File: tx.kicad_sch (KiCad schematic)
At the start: 52 parts, among them J7 SMA, Q1 PMOS, Q4 2NPN, T2 RF_BALUN, U12 MAX2831, U13 TXIF_BALUN, U16 DPDT

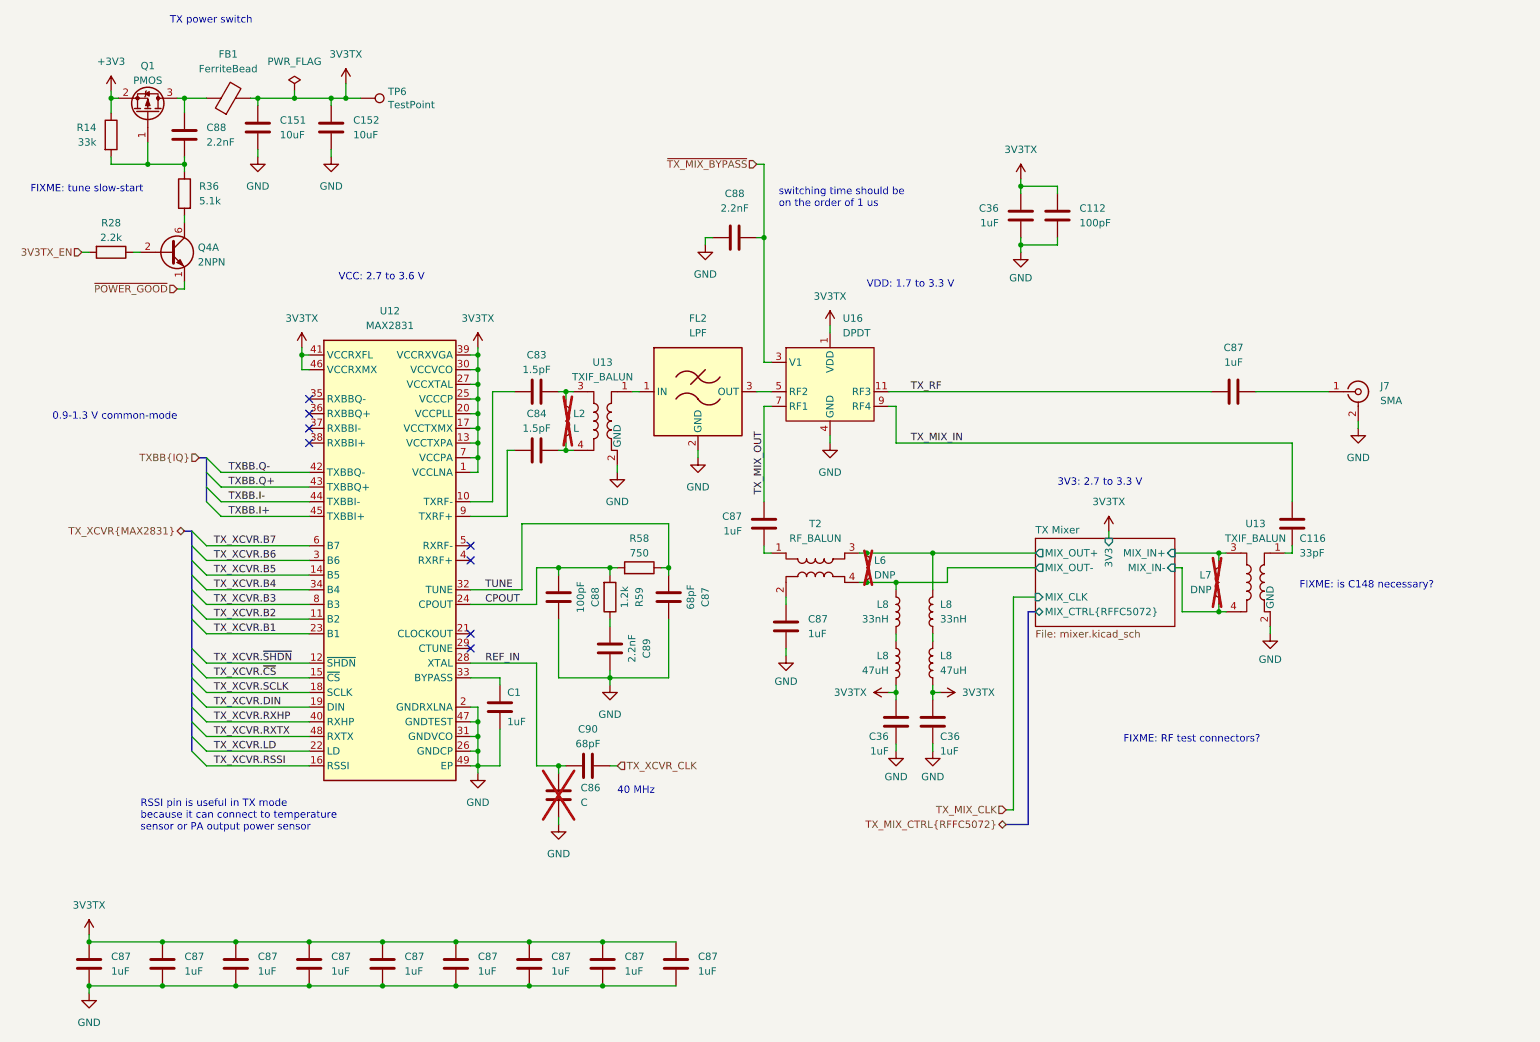
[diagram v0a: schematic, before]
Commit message: add regulator for analog 3.3 V supply
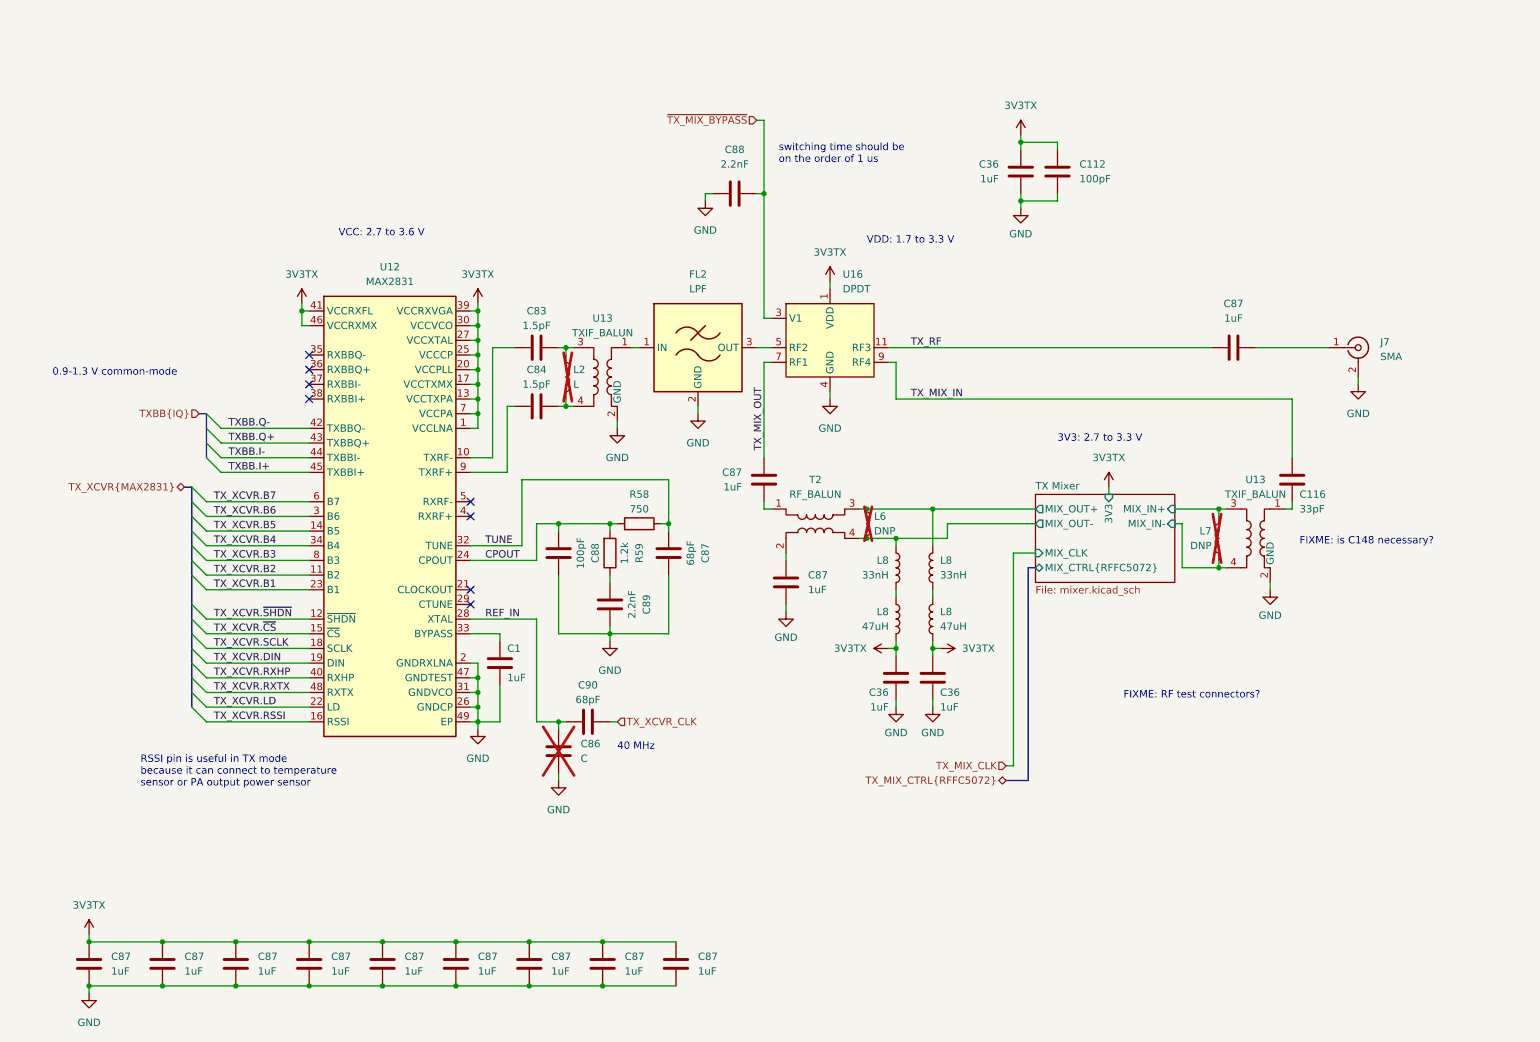
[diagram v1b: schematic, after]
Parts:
- removed C151, C152: 10uF, Capacitor_SMD:C_0603_1608Metric, symbol Device:C
- removed C88: 2.2nF, Capacitor_SMD:C_0201_0603Metric, symbol Device:C
- removed FB1: FerriteBead, symbol Device:FerriteBead
- removed Q1: PMOS, Package_TO_SOT_SMD:SOT-23-3, symbol Device:Q_PMOS_GSD
- removed Q4: 2NPN, Package_TO_SOT_SMD:SOT-363_SC-70-6, symbol Transistor_BJT:BC847BS
- removed R14: 33k, Resistor_SMD:R_0402_1005Metric, symbol Device:R
- removed R28: 2.2k, Resistor_SMD:R_0402_1005Metric, symbol Device:R
- removed R36: 5.1k, Resistor_SMD:R_0402_1005Metric, symbol Device:R
- removed TP6: TestPoint, TestPoint:TestPoint_Pad_D1.0mm, symbol Connector:TestPoint
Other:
- note removed: "FIXME: tune slow-start"
- note removed: "TX power switch"
- moved on the sheet: C1, C112, C116, C36, C83, C84, C86, C87, C88, C89, C90, FL2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

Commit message: add SWH two-way RF test connectors
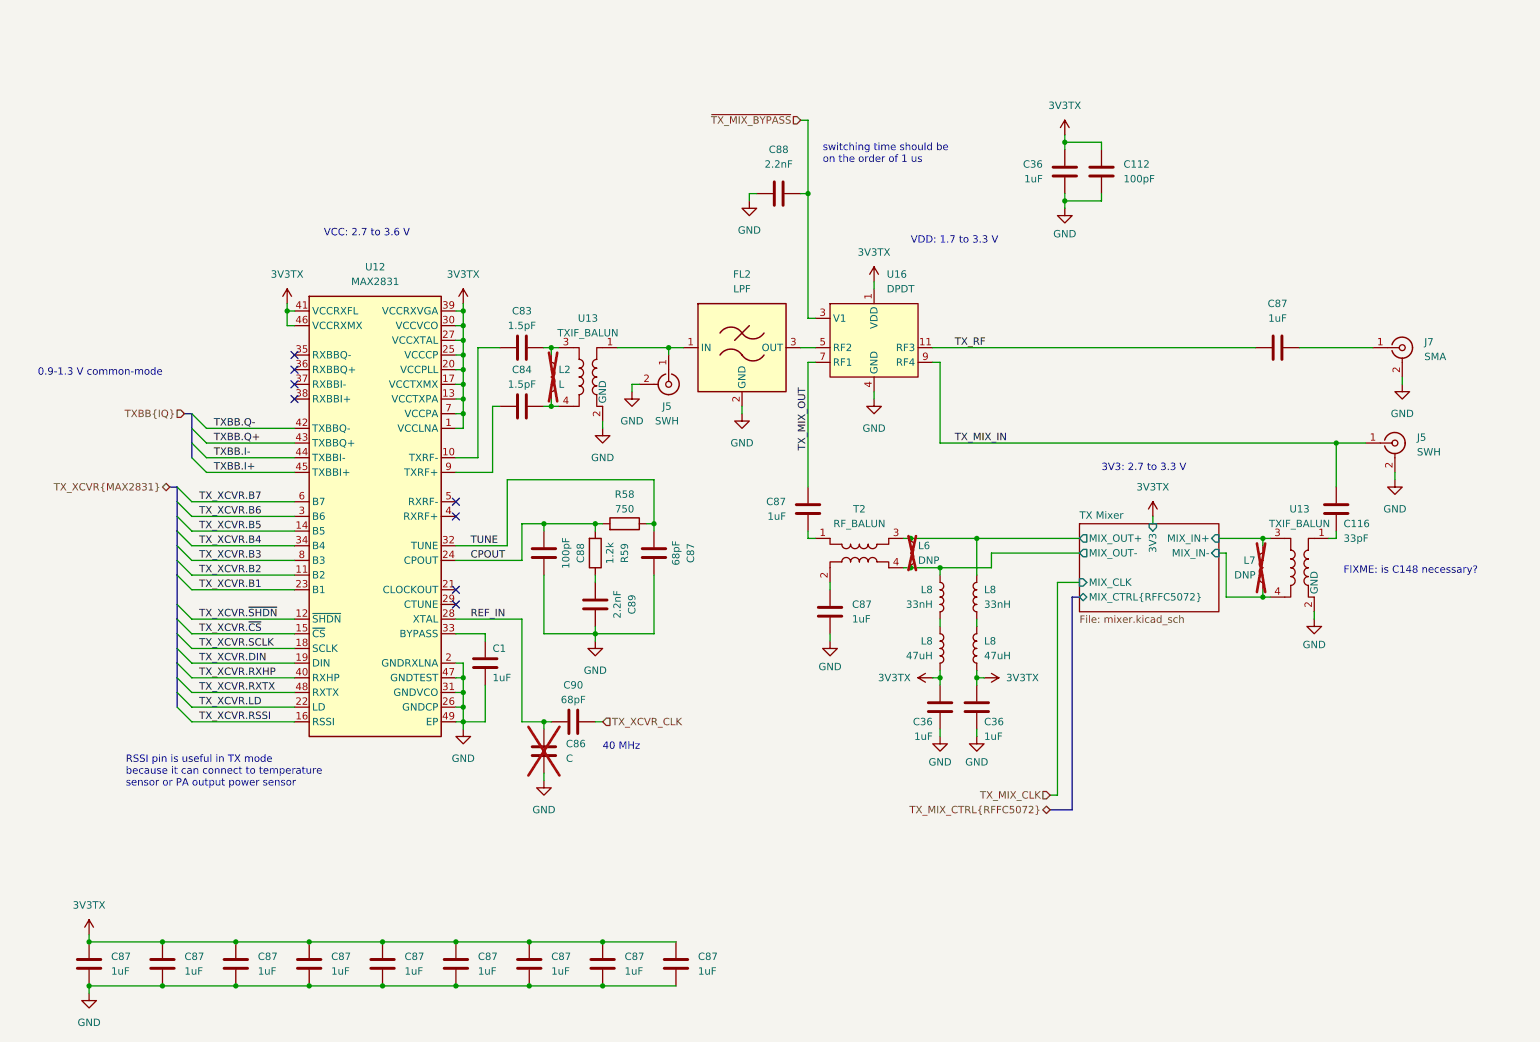
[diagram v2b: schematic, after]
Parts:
- added J5 (x2): SWH, symbol Connector:Conn_Coaxial
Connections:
- net GND: now also J5.2 (Ext), J5.2 (Ext)
- net TX_MIX_IN: now also J5.1 (In)
- net at FL2.1 (IN), U13.1: now also J5.1 (In)
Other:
- note removed: "FIXME: RF test connectors?"
- moved on the sheet: C1, C112, C116, C36, C83, C84, C86, C87, C88, C89, C90, FL2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

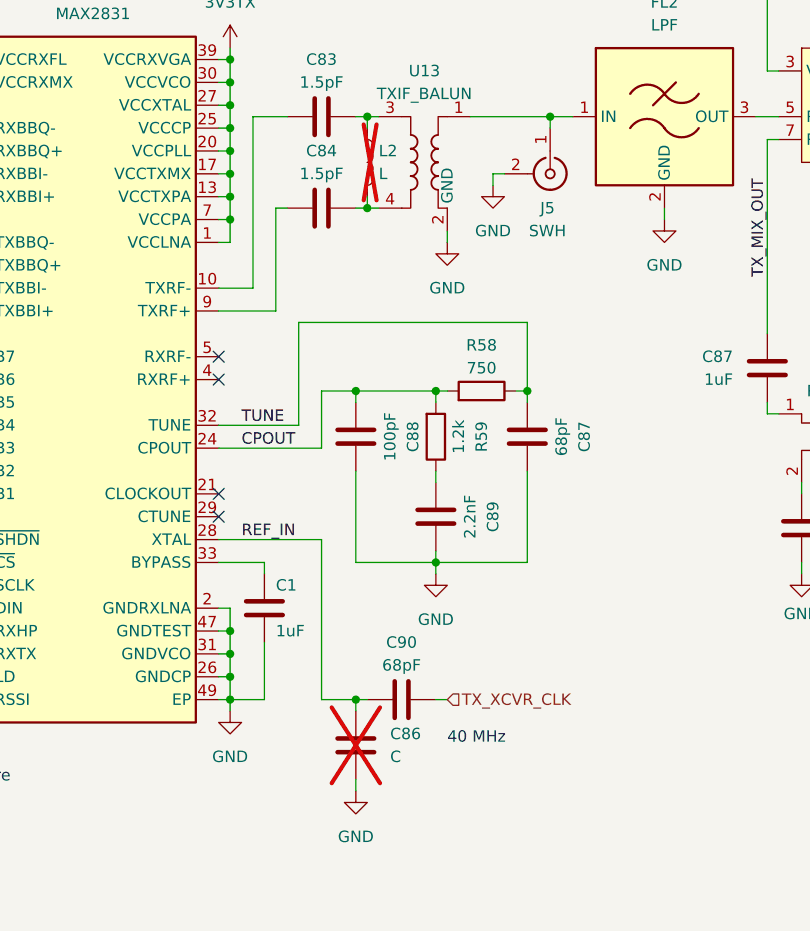
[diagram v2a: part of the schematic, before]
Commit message: update symbol metadata
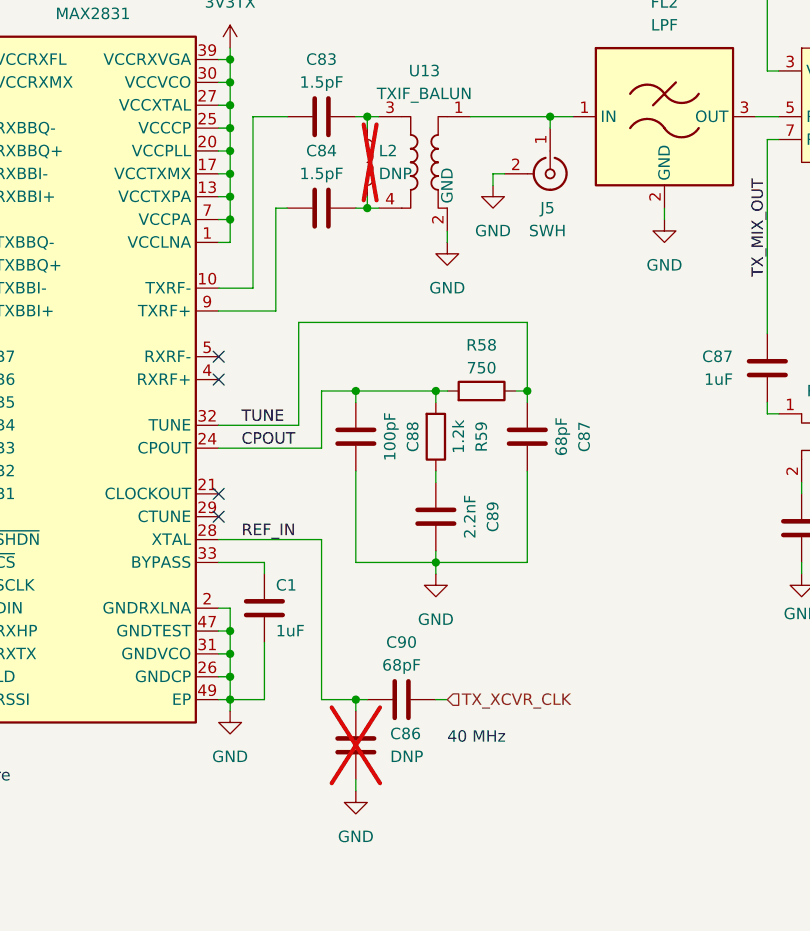
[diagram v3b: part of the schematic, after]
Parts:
- C86: value C -> DNP
- L2: value L -> DNP
- U12: Manufacturer (none) -> Analog Devices; Part Number (none) -> MAX2831ETM+T; Substitution (none) -> MAX2831ETM+, MAX2830ETM+T, MAX2830ETM+
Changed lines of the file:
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@@
       (effects (font (size 1.27 1.27)) (justify left))
     )
-    (property "Value" "L" (at 113.03 81.28 0)
+    (property "Value" "DNP" (at 113.03 81.28 0)
       (effects (font (size 1.27 1.27)) (justify left))
     )
@@
       (effects (font (size 1.27 1.27)) (justify left))
     )
-    (property "Value" "C" (at 114.3 146.05 0)
+    (property "Value" "DNP" (at 114.3 146.05 0)
       (effects (font (size 1.27 1.27)) (justify left))
     )
@@
     )
     (property "Part Number" "MXD8546FA" (at 167.64 74.93 90)
+      (effects (font (size 1.27 1.27)) hide)
+    )
+    (property "Description" "X-DPDT RF SWITCH" (at 167.64 74.93 0)
       (effects (font (size 1.27 1.27)) hide)
     )
@@
     (property "Datasheet" "https://www.analog.com/media/en/technical-documentation/data-sheets/MAX2831-MAX2832.pdf" (at 81.28 144.78 0)
       (effects (font (size 1.27 1.27) italic) hide)
+    )
+    (property "Manufacturer" "Analog Devices" (at 81.28 104.14 0)
+      (effects (font (size 1.27 1.27)) hide)
+    )
+    (property "Description" "IC RF TXRX WIFI 48WFQFN" (at 81.28 104.14 0)
+      (effects (font (size 1.27 1.27)) hide)
+    )
+    (property "Part Number" "MAX2831ETM+T" (at 81.28 104.14 0)
+      (effects (font (size 1.27 1.27)) hide)
+    )
+    (property "Substitution" "MAX2831ETM+, MAX2830ETM+T, MAX2830ETM+" (at 81.28 104.14 0)
+      (effects (font (size 1.27 1.27)) hide)
     )
     (pin "1")
@@
       (effects (font (size 1.27 1.27)) hide)
     )
+    (property "Description" "RF FILTER LOW PASS 2.45GHZ 0402" (at 144.78 74.93 0)
+      (effects (font (size 1.27 1.27)) hide)
+    )

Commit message: add SWH connector symbols
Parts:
- removed J5 (x2): SWH, symbol Connector:Conn_Coaxial
- added J5 (x2): SWH, symbol radio:Conn_Coaxial_MM8930-2620
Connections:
- net GND: now also J5.3 (Ext), J5.3 (Ext)
- net TX_MIX_IN: now also J5.1 (C); no longer C116.1
- net at U13.1: now also J5.1 (C); no longer FL2.1 (IN)
- new net: C116.1, J5.2 (R)
- new net: FL2.1 (IN), J5.2 (R)
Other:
- moved on the sheet: C112, C116, C36, C87, C88, FL2, J7, L6, L7, L8, T2, U13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
